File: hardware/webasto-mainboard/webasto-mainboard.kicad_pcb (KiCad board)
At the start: 4 copper layers, 86.8 x 76 mm, 96 parts, among them J1 Console FTDI, J2 I2C, Q1 DMG2301L, Q10 SUD50P04-08, Q11 SUD50P04-08, Q12 SUD50P04-08, Q13 SUD50P04-08, Q14 SUD50P04-08, Q15 2N7002, Q16 2N7002, Q17 2N7002, Q18 2N7002, Q2 2N7002, Q3 2N7002, Q4 2N7002, Q5 SUD50P04-08, Q6 SUD50P04-08, Q7 SUD50P04-08, Q8 SSM3J374R, Q9 2N7002, U1 CY15E004J, U10 MCP2557FD-xMF, U2 PicoW, U3 LM4040DIM3-3.0, U4 MC33660BEFR2, U5 Voltage Regulator, U6 LM7805_TO220, U7 INA219BxDCN, U8 TCA9534, U9 MCP2517FD, X1 ASV-20.000MHZ-EJ-T

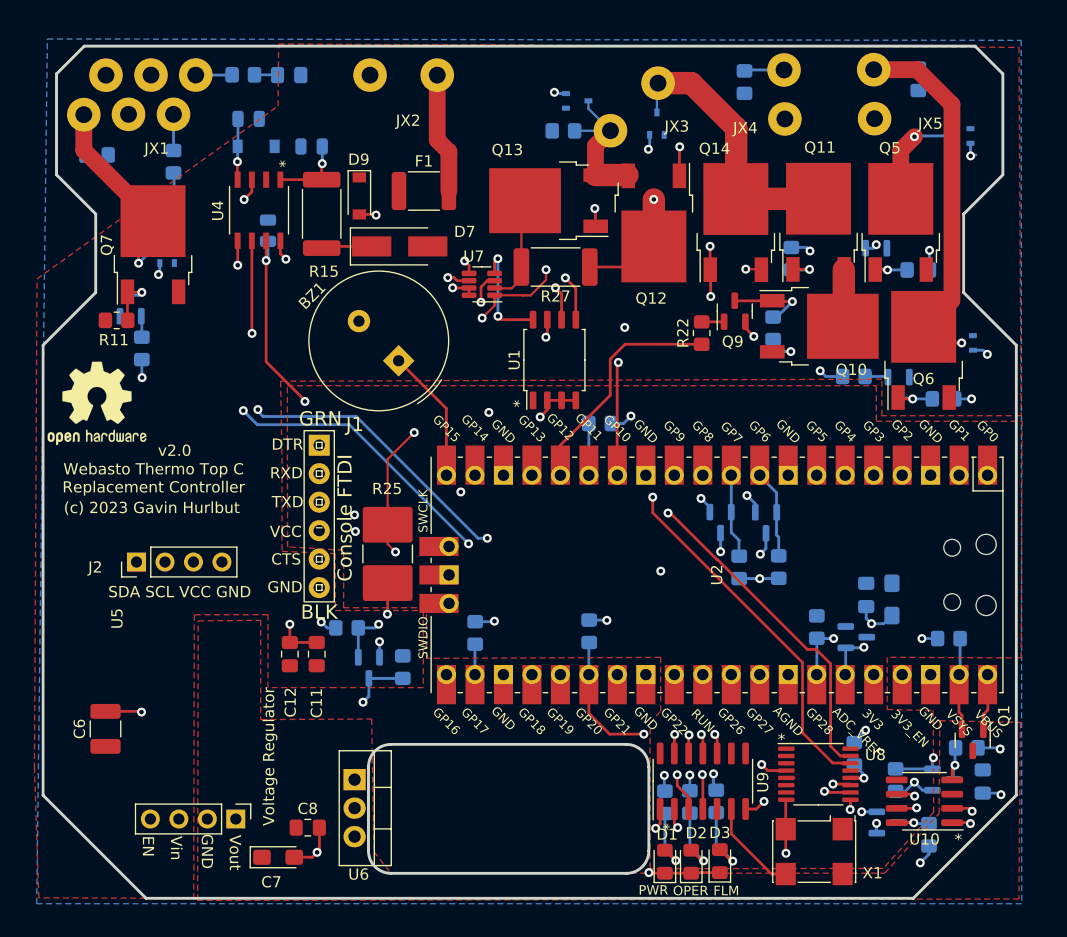
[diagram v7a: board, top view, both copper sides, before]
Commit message: Removing KLine and I2C from X1, reattaching the external IOs.
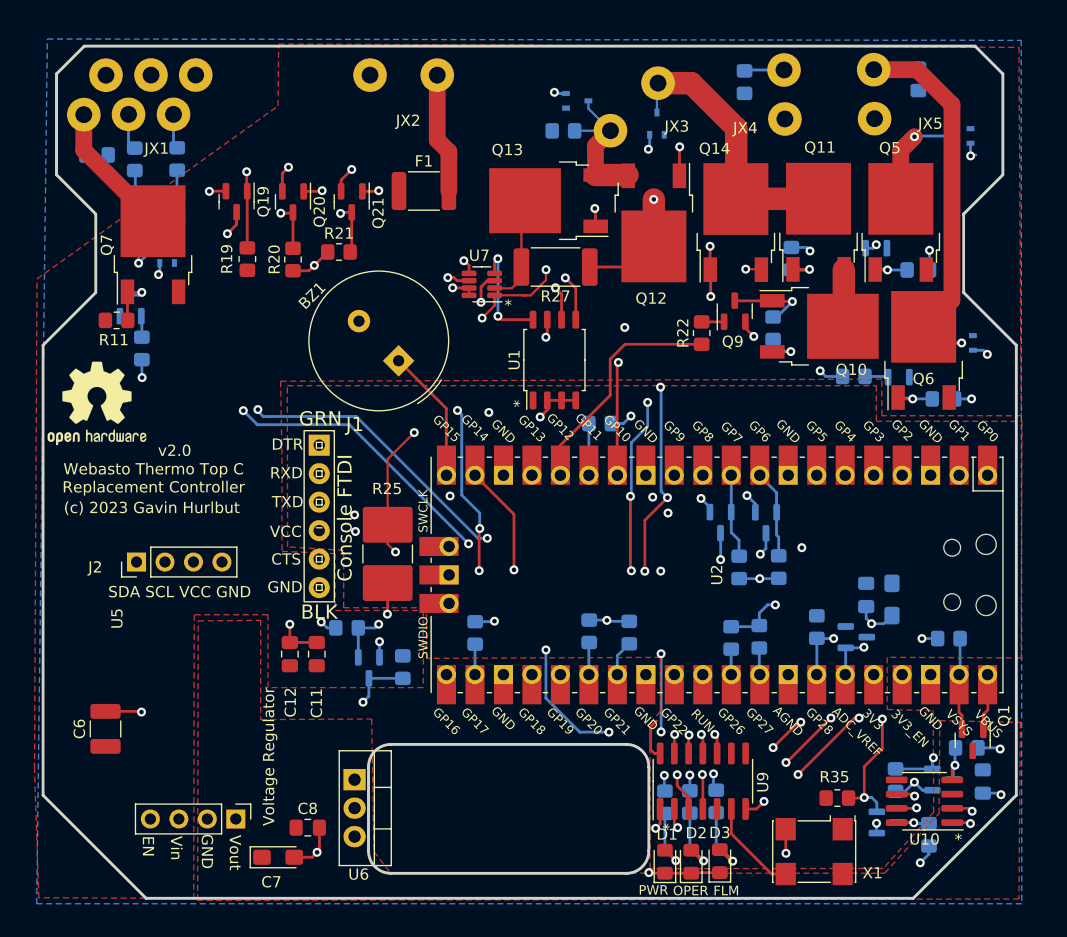
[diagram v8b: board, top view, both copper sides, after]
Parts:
- removed C3: 1nF, Capacitor_SMD:C_0805_2012Metric
- removed C4: 10nF, Capacitor_SMD:C_0805_2012Metric
- removed C5: 5nF, Capacitor_SMD:C_0805_2012Metric
- removed D7: BYS10-35, Diode_SMD:D_SMA_Handsoldering
- removed D8: BZT52C27-7-F, Diode_SMD:D_SOD-123
- removed D9: MMSZ5260C-E3-08, Diode_SMD:D_SOD-123
- removed R15: 510R 2W, Resistor_SMD:R_2512_6332Metric_Pad1.40x3.35mm_HandSolder
- removed U4: MC33660BEFR2, UltraLibrarian:MC33660BEFR2
- removed U8: TCA9534, Package_SO:TSSOP-16_4.4x5mm_P0.65mm
- added Q19: 2N7002, Package_TO_SOT_SMD:SOT-23, F.Cu at (117.5, 67.4)
- added Q20: 2N7002, Package_TO_SOT_SMD:SOT-23, F.Cu at (122.5, 67.4)
- added Q21: 2N7002, Package_TO_SOT_SMD:SOT-23, F.Cu at (127.7, 67.4)
- added R16: 10k, Resistor_SMD:R_0805_2012Metric_Pad1.20x1.40mm_HandSolder, B.Cu at (152.5, 105.8)
- added R17: 10k, Resistor_SMD:R_0805_2012Metric_Pad1.20x1.40mm_HandSolder, B.Cu at (161.6, 106.3)
- added R18: 10k, Resistor_SMD:R_0805_2012Metric_Pad1.20x1.40mm_HandSolder, B.Cu at (164.1, 106.2)
- added R19: 10k, Resistor_SMD:R_0805_2012Metric_Pad1.20x1.40mm_HandSolder, F.Cu at (118.4, 72.5)
- added R20: 10k, Resistor_SMD:R_0805_2012Metric_Pad1.20x1.40mm_HandSolder, F.Cu at (122.5, 72.6)
- added R21: 10k, Resistor_SMD:R_0805_2012Metric_Pad1.20x1.40mm_HandSolder, F.Cu at (126.6, 71.9)
- R35: moved to F.Cu
- moved C14 15.3 mm to (112.1, 67.7), turned to 90 degrees
- moved R38 9.54 mm to (112.2, 63.6), turned to -90 degrees
- moved R35 4.23 mm to (171.0, 120.6), turned to 0 degrees
- moved C15 3.46 mm to (108.4, 67.7)
- moved R39 3.46 mm to (108.4, 63.6)
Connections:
- JX1 pad 1: CAN_HI -> START_RUN
- JX1 pad 2: KLine -> IGNITION_SENSE
- JX1 pad 3: SDA -> ~{EMERGENCY_STOP}
- JX1 pad 4: CAN_LO -> CAN_HI
- JX1 pad 5: SCL -> CAN_LO
- U2 pad 19: unconnected-(U2-Pad19) -> CAN_SOF
- U2 pad 27: unconnected-(U2-Pad27) -> EMERGENCY_STOP_3V
- U2 pad 31: unconnected-(U2-Pad31) -> IGNITION_SENSE_3V
- U2 pad 32: unconnected-(U2-Pad32) -> START_RUN_3V
- U2 pad 4: unconnected-(U2-Pad4) -> FlameLED
- U2 pad 5: KLineEN -> OperatingLED
- U2 pad 6: KLineTX -> PowerLED
- U2 pad 7: KLineRX -> ~{CAN_EN_3V}
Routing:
- net IGNITION_SENSE_3V: track 0.00 -> 76.6 mm, vias 0 -> 4
- net START_RUN_3V: track 0.00 -> 75.1 mm, vias 0 -> 4
- net SDA: track 170.1 -> 97.5 mm
- net SCL: track 162.5 -> 90.9 mm
- net KLineEN: track 70.0 -> 0.00 mm, vias 1 -> 0
- net KLineTX: track 69.6 -> 0.00 mm, vias 1 -> 0
- net KLineRX: track 67.4 -> 0.00 mm, vias 1 -> 0
- net EMERGENCY_STOP_3V: track 0.00 -> 64.0 mm, vias 0 -> 4
- net ~{CAN_EN_3V}: track 7.17 -> 39.1 mm, vias 2 -> 3
- net CAN_SOF: track 14.1 -> 41.1 mm, vias 2 -> 4
- net ~{EMERGENCY_STOP}: track 0.00 -> 26.7 mm, vias 0 -> 1
- net IGNITION_SENSE: track 0.00 -> 26.5 mm, vias 0 -> 1
- net FlameLED: track 14.2 -> 40.2 mm, vias 2 -> 3
- net START_RUN: track 0.00 -> 24.2 mm, vias 0 -> 1
- net OperatingLED: track 16.3 -> 39.3 mm, vias 2 -> 3
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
